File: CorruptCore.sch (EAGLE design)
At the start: 85 parts, among them IC1 MEGA8-P, K1 DTS-3, K10 DTS-3, K11 DTS-3, K12 DTS-3, K13 DTS-3, K14 DTS-3, K15 DTS-3, K16 DTS-3, K2 DTS-3, K3 DTS-3, K4 DTS-3, K5 DTS-3, K6 DTS-3, K7 DTS-3, K8 DTS-3, K9 DTS-3, Y1 16MHz

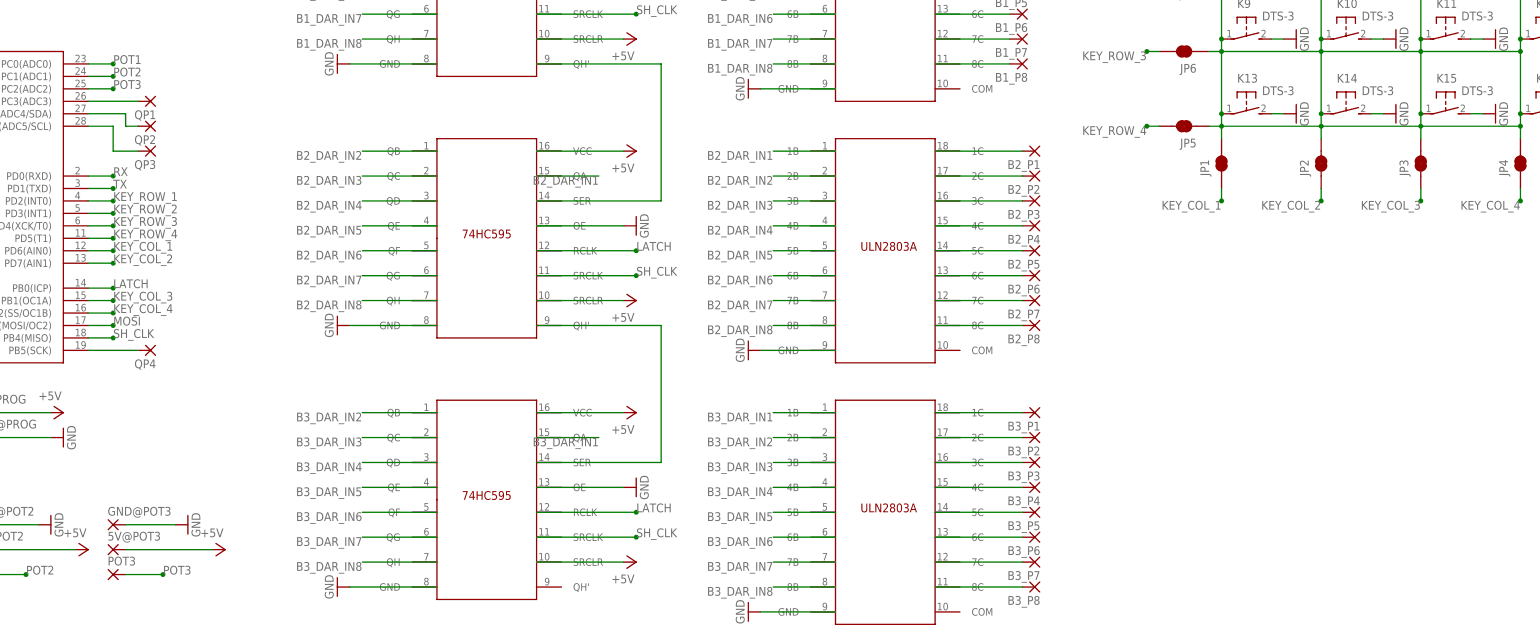
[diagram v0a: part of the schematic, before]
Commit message: -forgot to include darlington transistors for the quick corrupt pins
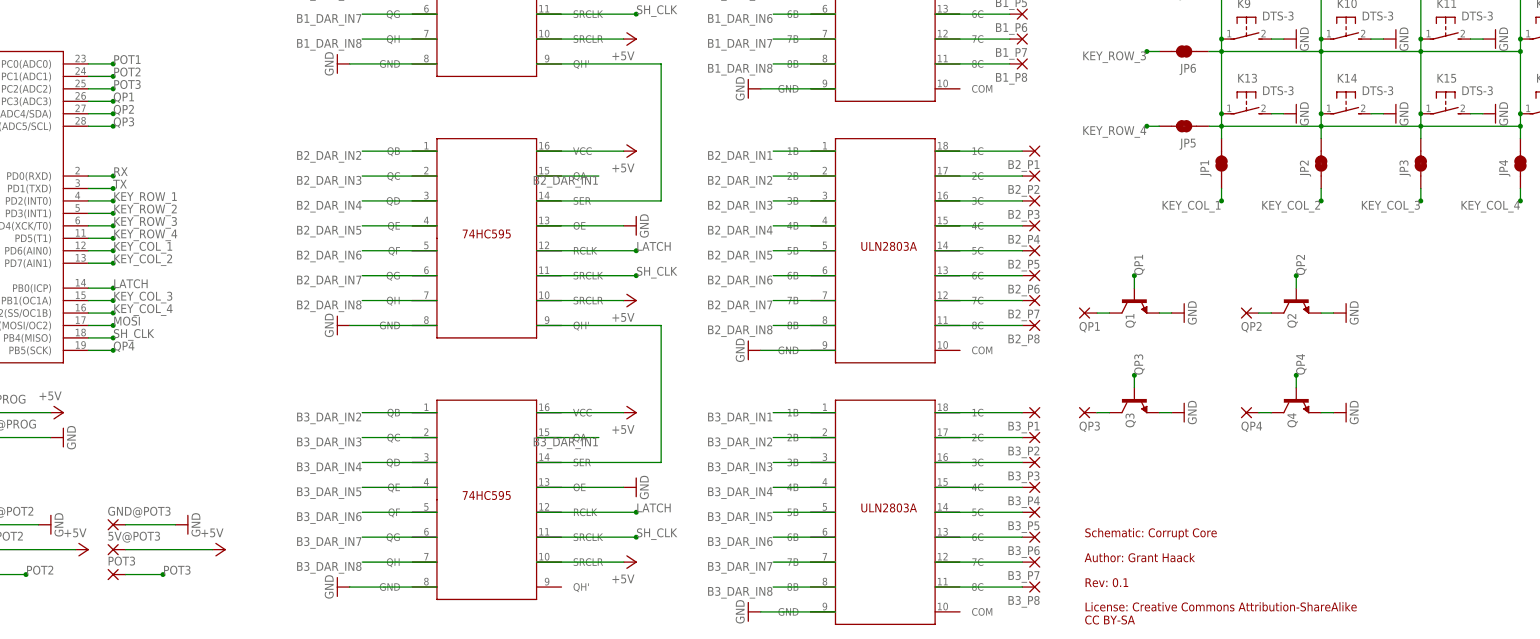
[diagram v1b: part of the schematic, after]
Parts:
- added Q1, Q2, Q3, Q4: TRANS_NPN-MMBTA42, SparkFun-DiscreteSemi:TRANS_NPN-MMBTA42
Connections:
- new net N$12: Q4.C, QP4.P
- new net QP1: IC1.PC3(ADC3), Q1.B
- new net QP2: IC1.PC4(ADC4/SDA), Q2.B
- new net QP3: IC1.PC5(ADC5/SCL), Q3.B
- net GND: now also Q1.E, Q2.E, Q3.E, Q4.E
- net N$10: now also Q2.C, QP2.P; no longer IC1.PC3(ADC3), QP1.P
- net N$11: now also Q3.C; no longer IC1.PC5(ADC5/SCL)
- net N$8: now also Q1.C, QP1.P; no longer IC1.PC4(ADC4/SDA), QP2.P
- net QP4: now also Q4.B; no longer QP4.P
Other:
- note added: "Author: Grant Haack"
- note added: "License: Creative Commons Attribution-ShareAlike CC BY-SA"
- note added: "Rev: 0.1"
- note added: "Schematic: Corrupt Core"
- moved on the sheet: QP1, QP2, QP3, QP4
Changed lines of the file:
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@@
 <part name="GND31" library="supply1" library_urn="urn:adsk.eagle:library:371" deviceset="GND" device=""/>
 <part name="GND32" library="supply1" library_urn="urn:adsk.eagle:library:371" deviceset="GND" device=""/>
-<part name="QP1" library="wirepad" library_urn="urn:adsk.eagle:library:412" deviceset="2,54/1,1" device=""/>
-<part name="QP2" library="wirepad" library_urn="urn:adsk.eagle:library:412" deviceset="2,54/1,1" device=""/>
-<part name="QP3" library="wirepad" library_urn="urn:adsk.eagle:library:412" deviceset="2,54/1,1" device=""/>
-<part name="QP4" library="wirepad" library_urn="urn:adsk.eagle:library:412" deviceset="2,54/1,1" device=""/>
 <part name="JP1" library="SparkFun-Jumpers" library_urn="urn:adsk.eagle:library:528" deviceset="JUMPER-SMT_2_NC_TRACE" device="_NO-SILK" value=""/>
 <part name="JP2" library="SparkFun-Jumpers" library_urn="urn:adsk.eagle:library:528" deviceset="JUMPER-SMT_2_NC_TRACE" device="_NO-SILK" value=""/>
@@
 <part name="P+13" library="supply1" library_urn="urn:adsk.eagle:library:371" deviceset="+5V" device=""/>
 <part name="P+14" library="supply1" library_urn="urn:adsk.eagle:library:371" deviceset="+5V" device=""/>
+<part name="Q1" library="SparkFun-DiscreteSemi" library_urn="urn:adsk.eagle:library:514" deviceset="TRANS_NPN" device="-MMBTA42" value=""/>
+<part name="Q2" library="SparkFun-DiscreteSemi" library_urn="urn:adsk.eagle:library:514" deviceset="TRANS_NPN" device="-MMBTA42" value=""/>
+<part name="Q3" library="SparkFun-DiscreteSemi" library_urn="urn:adsk.eagle:library:514" deviceset="TRANS_NPN" device="-MMBTA42" value=""/>
+<part name="Q4" library="SparkFun-DiscreteSemi" library_urn="urn:adsk.eagle:library:514" deviceset="TRANS_NPN" device="-MMBTA42" value=""/>
+<part name="GND39" library="supply1" library_urn="urn:adsk.eagle:library:371" deviceset="GND" device=""/>
+<part name="GND40" library="supply1" library_urn="urn:adsk.eagle:library:371" deviceset="GND" device=""/>
+<part name="GND41" library="supply1" library_urn="urn:adsk.eagle:library:371" deviceset="GND" device=""/>
+<part name="GND42" library="supply1" library_urn="urn:adsk.eagle:library:371" deviceset="GND" device=""/>
+<part name="QP1" library="wirepad" library_urn="urn:adsk.eagle:library:412" deviceset="2,54/1,1" device=""/>
+<part name="QP2" library="wirepad" library_urn="urn:adsk.eagle:library:412" deviceset="2,54/1,1" device=""/>
+<part name="QP3" library="wirepad" library_urn="urn:adsk.eagle:library:412" deviceset="2,54/1,1" device=""/>
+<part name="QP4" library="wirepad" library_urn="urn:adsk.eagle:library:412" deviceset="2,54/1,1" device=""/>
 </parts>
 <sheets>
 <sheet>
 <plain>
+<text x="269.24" y="-58.42" size="1.778" layer="94">Schematic: Corrupt Core</text>
+<text x="269.24" y="-63.5" size="1.778" layer="94">Author: Grant Haack</text>
+<text x="269.24" y="-68.58" size="1.778" layer="94">Rev: 0.1</text>
+<text x="269.24" y="-76.2" size="1.778" layer="94">License: Creative Commons Attribution-ShareAlike
+CC BY-SA</text>
 </plain>
 <instances>
@@
 <instance part="GND31" gate="1" x="15.24" y="-27.94"/>
 <instance part="GND32" gate="1" x="40.64" y="73.66" rot="R90"/>
-<instance part="QP1" gate="1" x="78.74" y="30.48" rot="R180"/>
-<instance part="QP2" gate="1" x="78.74" y="25.4" rot="R180"/>
-<instance part="QP3" gate="1" x="78.74" y="20.32" rot="R180"/>
-<instance part="QP4" gate="1" x="78.74" y="-20.32" rot="R180"/>
 <instance part="JP1" gate="G$1" x="297.18" y="17.78" rot="R90"/>
 <instance part="JP2" gate="G$1" x="317.5" y="17.78" rot="R90"/>
@@
 <instance part="P+13" gate="1" x="66.04" y="-60.96" rot="R270"/>
 <instance part="P+14" gate="1" x="38.1" y="-60.96" rot="R270"/>
+<instance part="Q1" gate="G$1" x="279.4" y="-10.16" rot="MR270"/>
+<instance part="Q2" gate="G$1" x="312.42" y="-10.16" rot="MR270"/>
+<instance part="Q3" gate="G$1" x="279.4" y="-30.48" rot="MR270"/>
+<instance part="Q4" gate="G$1" x="312.42" y="-30.48" rot="MR270"/>
+<instance part="GND39" gate="1" x="289.56" y="-12.7" rot="MR270"/>
+<instance part="GND40" gate="1" x="322.58" y="-12.7" rot="MR270"/>
+<instance part="GND41" gate="1" x="289.56" y="-33.02" rot="MR270"/>
+<instance part="GND42" gate="1" x="322.58" y="-33.02" rot="MR270"/>
+<instance part="QP1" gate="1" x="269.24" y="-12.7" rot="MR180"/>
+<instance part="QP2" gate="1" x="302.26" y="-12.7" rot="MR180"/>
+<instance part="QP3" gate="1" x="269.24" y="-33.02" rot="MR180"/>
+<instance part="QP4" gate="1" x="302.26" y="-33.02" rot="MR180"/>
 </instances>
 <busses>
@@
 <wire x1="17.78" y1="-55.88" x2="27.94" y2="-55.88" width="0.1524" layer="91"/>
 <pinref part="GND38" gate="1" pin="GND"/>
+</segment>
+<segment>
+<pinref part="Q1" gate="G$1" pin="E"/>
+<pinref part="GND39" gate="1" pin="GND"/>
+<wire x1="287.02" y1="-12.7" x2="284.48" y2="-12.7" width="0.1524" layer="91"/>
+</segment>
+<segment>
+<pinref part="Q2" gate="G$1" pin="E"/>
+<pinref part="GND40" gate="1" pin="GND"/>
+<wire x1="320.04" y1="-12.7" x2="317.5" y2="-12.7" width="0.1524" layer="91"/>
+</segment>
+<segment>
+<pinref part="Q3" gate="G$1" pin="E"/>
+<pinref part="GND41" gate="1" pin="GND"/>
+<wire x1="287.02" y1="-33.02" x2="284.48" y2="-33.02" width="0.1524" layer="91"/>
+</segment>
+<segment>
+<pinref part="Q4" gate="G$1" pin="E"/>
+<pinref part="GND42" gate="1" pin="GND"/>
+<wire x1="320.04" y1="-33.02" x2="317.5" y2="-33.02" width="0.1524" layer="91"/>
 </segment>
 </net>
@@
 <segment>
 <pinref part="IC1" gate="G$1" pin="PB5(SCK)"/>
-<pinref part="QP4" gate="1" pin="P"/>
-<wire x1="66.04" y1="-20.32" x2="76.2" y2="-20.32" width="0.1524" layer="91"/>
+<wire x1="66.04" y1="-20.32" x2="71.12" y2="-20.32" width="0.1524" layer="91"/>
+<junction x="71.12" y="-20.32"/>
+<label x="71.12" y="-20.32" size="1.778" layer="95"/>
+</segment>
+<segment>
+<pinref part="Q4" gate="G$1" pin="B"/>
+<wire x1="312.42" y1="-27.94" x2="312.42" y2="-25.4" width="0.1524" layer="91"/>
+<junction x="312.42" y="-25.4"/>
+<label x="312.42" y="-25.4" size="1.778" layer="95" rot="MR90"/>
 </segment>
 </net>
@@
 </segment>
 </net>
-<net name="N$8" class="0">
+<net name="QP2" class="0">
 <segment>
 <pinref part="IC1" gate="G$1" pin="PC4(ADC4/SDA)"/>
-<wire x1="66.04" y1="27.94" x2="73.66" y2="27.94" width="0.1524" layer="91"/>
-<wire x1="73.66" y1="27.94" x2="73.66" y2="25.4" width="0.1524" layer="91"/>
-<pinref part="QP2" gate="1" pin="P"/>
-<wire x1="73.66" y1="25.4" x2="76.2" y2="25.4" width="0.1524" layer="91"/>
-</segment>
-</net>
-<net name="N$10" class="0">
+<wire x1="66.04" y1="27.94" x2="71.12" y2="27.94" width="0.1524" layer="91"/>
+<junction x="71.12" y="27.94"/>
+<label x="71.12" y="27.94" size="1.778" layer="95"/>
+</segment>
+<segment>
+<pinref part="Q2" gate="G$1" pin="B"/>
+<wire x1="312.42" y1="-7.62" x2="312.42" y2="-5.08" width="0.1524" layer="91"/>
+<junction x="312.42" y="-5.08"/>
+<label x="312.42" y="-5.08" size="1.778" layer="95" rot="MR90"/>
+</segment>
+</net>
+<net name="QP1" class="0">
 <segment>
 <pinref part="IC1" gate="G$1" pin="PC3(ADC3)"/>
-<pinref part="QP1" gate="1" pin="P"/>
-<wire x1="66.04" y1="30.48" x2="76.2" y2="30.48" width="0.1524" layer="91"/>
-</segment>
-</net>
-<net name="N$11" class="0">
+<wire x1="66.04" y1="30.48" x2="71.12" y2="30.48" width="0.1524" layer="91"/>
+<junction x="71.12" y="30.48"/>
+<label x="71.12" y="30.48" size="1.778" layer="95"/>
+</segment>
+<segment>
+<pinref part="Q1" gate="G$1" pin="B"/>
+<wire x1="279.4" y1="-7.62" x2="279.4" y2="-5.08" width="0.1524" layer="91"/>
+<junction x="279.4" y="-5.08"/>
+<label x="279.4" y="-5.08" size="1.778" layer="95" rot="MR90"/>
+</segment>
+</net>
+<net name="QP3" class="0">
 <segment>
 <pinref part="IC1" gate="G$1" pin="PC5(ADC5/SCL)"/>
 <wire x1="66.04" y1="25.4" x2="71.12" y2="25.4" width="0.1524" layer="91"/>
-<wire x1="71.12" y1="25.4" x2="71.12" y2="20.32" width="0.1524" layer="91"/>
+<junction x="71.12" y="25.4"/>
+<label x="71.12" y="25.4" size="1.778" layer="95"/>
+</segment>
+<segment>
+<pinref part="Q3" gate="G$1" pin="B"/>
+<wire x1="279.4" y1="-27.94" x2="279.4" y2="-25.4" width="0.1524" layer="91"/>
+<junction x="279.4" y="-25.4"/>
+<label x="279.4" y="-25.4" size="1.778" layer="95" rot="MR90"/>
+</segment>
+</net>
+<net name="N$8" class="0">
+<segment>
+<pinref part="Q1" gate="G$1" pin="C"/>
+<wire x1="274.32" y1="-12.7" x2="271.78" y2="-12.7" width="0.1524" layer="91"/>
+<pinref part="QP1" gate="1" pin="P"/>
+</segment>
+</net>
+<net name="N$10" class="0">
+<segment>
+<pinref part="Q2" gate="G$1" pin="C"/>
+<wire x1="307.34" y1="-12.7" x2="304.8" y2="-12.7" width="0.1524" layer="91"/>
+<pinref part="QP2" gate="1" pin="P"/>
+</segment>
+</net>
+<net name="N$11" class="0">
+<segment>
+<pinref part="Q3" gate="G$1" pin="C"/>
+<wire x1="274.32" y1="-33.02" x2="271.78" y2="-33.02" width="0.1524" layer="91"/>
 <pinref part="QP3" gate="1" pin="P"/>
-<wire x1="71.12" y1="20.32" x2="76.2" y2="20.32" width="0.1524" layer="91"/>
+</segment>
+</net>
+<net name="N$12" class="0">
+<segment>
+<pinref part="Q4" gate="G$1" pin="C"/>
+<wire x1="307.34" y1="-33.02" x2="304.8" y2="-33.02" width="0.1524" layer="91"/>
+<pinref part="QP4" gate="1" pin="P"/>
 </segment>
 </net>
@@
 </drawing>
 <compatibility>
+<note version="6.3" minversion="6.2.2" severity="warning">
+Since Version 6.2.2 text objects can contain more than one line,
+which will not be processed correctly with this version.
+</note>
 <note version="8.2" severity="warning">
 Since Version 8.2, Eagle supports online libraries. The ids

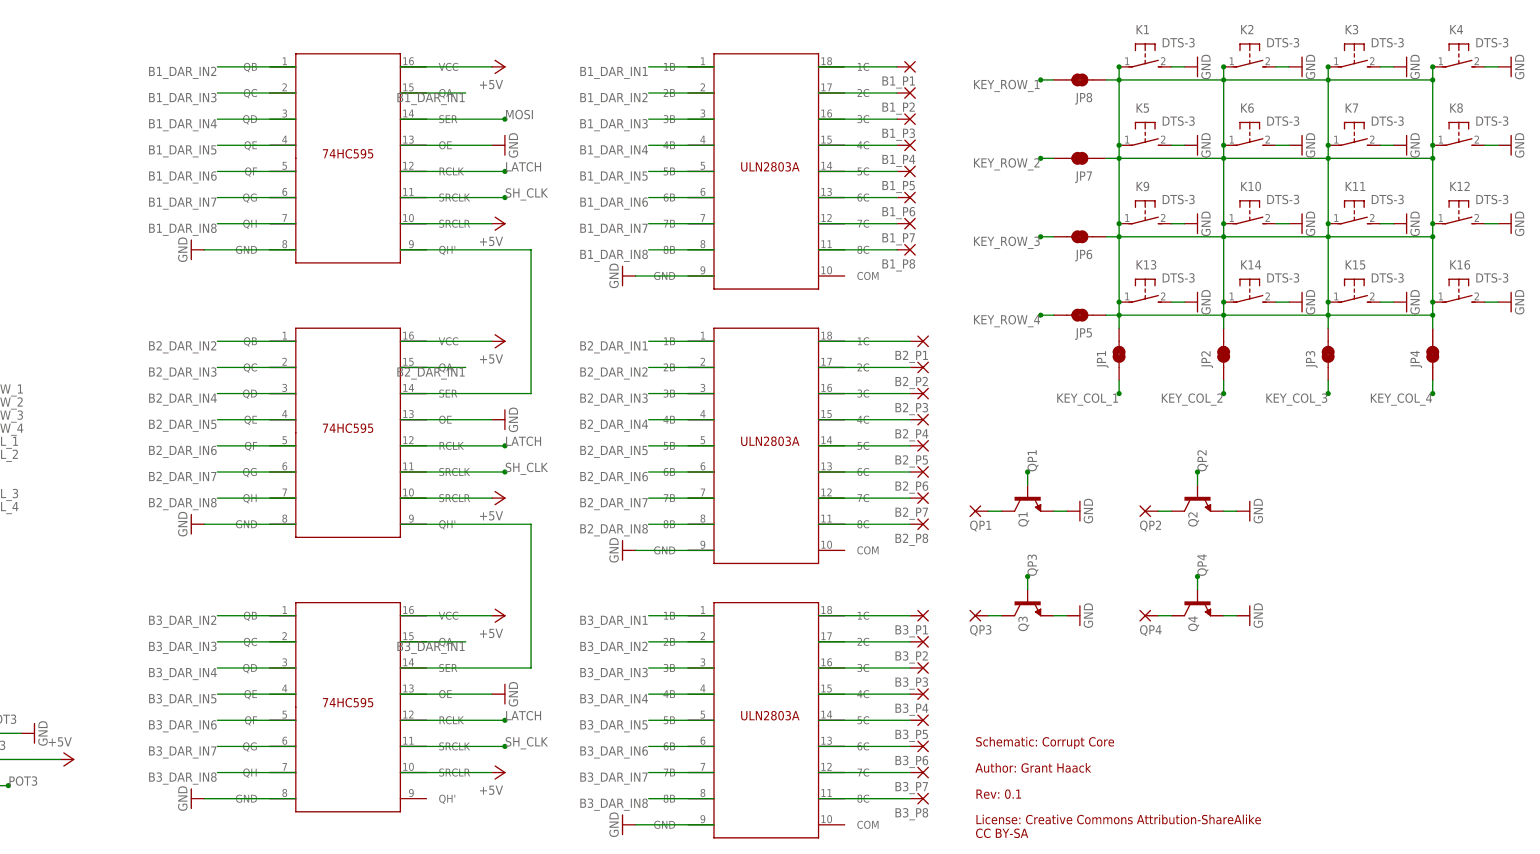
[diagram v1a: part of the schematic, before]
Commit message: -added a PNG of the schematic -small amounts of schematic cleaning
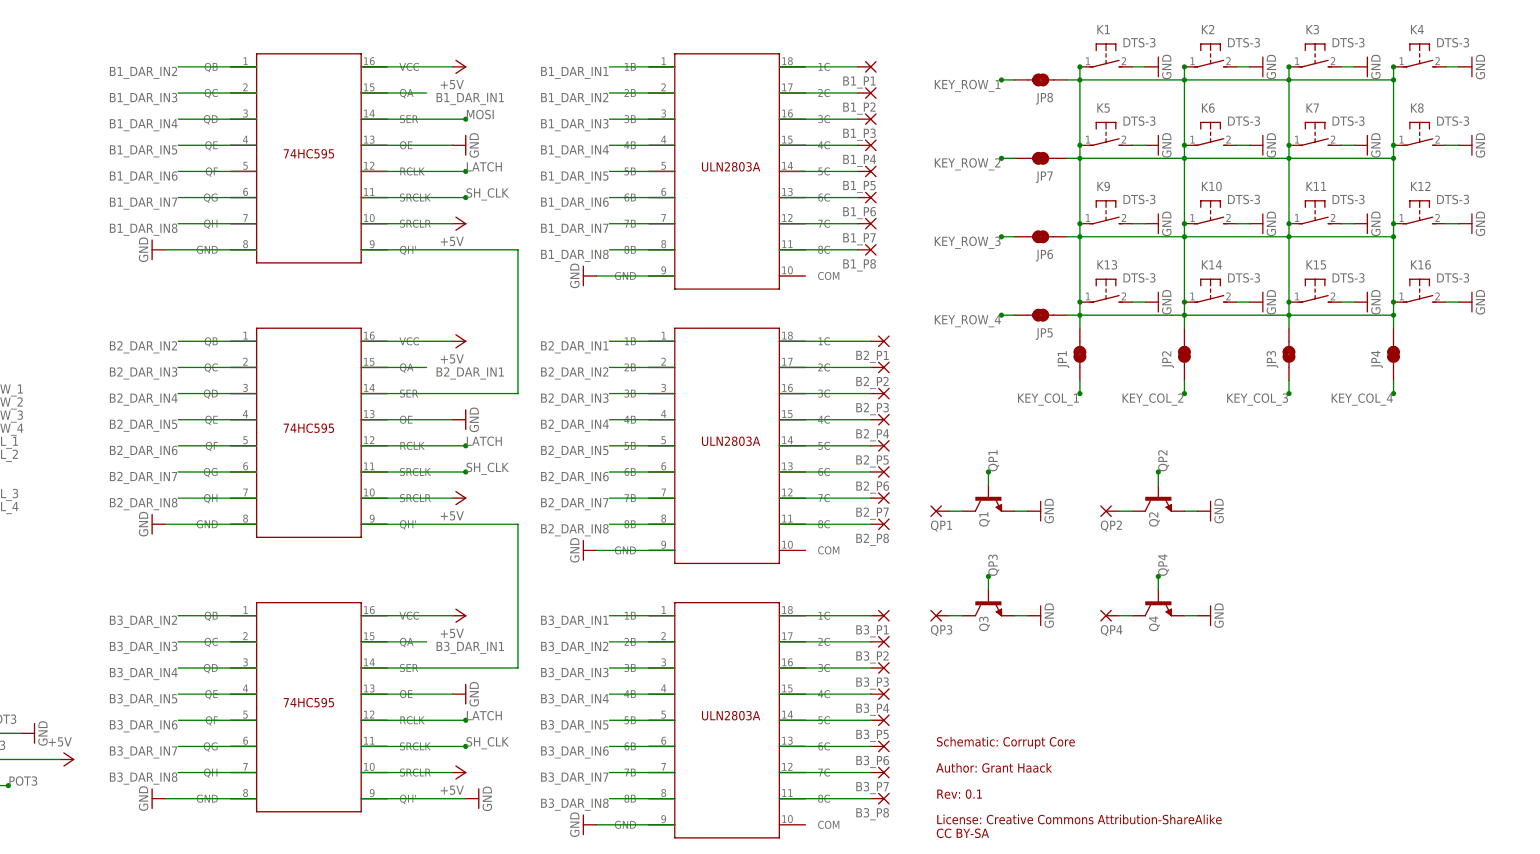
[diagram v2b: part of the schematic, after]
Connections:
- net GND: now also U$5.QH'
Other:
- moved on the sheet: B1_P1, B1_P2, B1_P3, B1_P4, B1_P5, B1_P6, B1_P7, B1_P8, B2_P1, B2_P2, B2_P3, B2_P4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
